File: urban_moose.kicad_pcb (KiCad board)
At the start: 2 copper layers, 27.4 x 49.5 mm, 52 parts, among them P1 SWD, P2 EXT, P3 ANT, Q1 MOSFET_N, Q2 MOSFET_N, SW1 SW_PUSH, U1 nRF51822-QFAA, U2 DS18B20, U3 BMP180, U4 Si1145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

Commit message: Update URL text to um2
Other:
- board text added: "timhawes.com/um2"
- board text removed: "timhawes.com/um1"
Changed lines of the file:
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@@
     )
   )
-  (gr_text timhawes.com/um1 (at 134.62 95.25 90) (layer B.SilkS)
+  (gr_text timhawes.com/um2 (at 134.62 95.25 90) (layer B.SilkS)
     (effects (font (size 1.5 1.5) (thickness 0.3)) (justify mirror))
   )

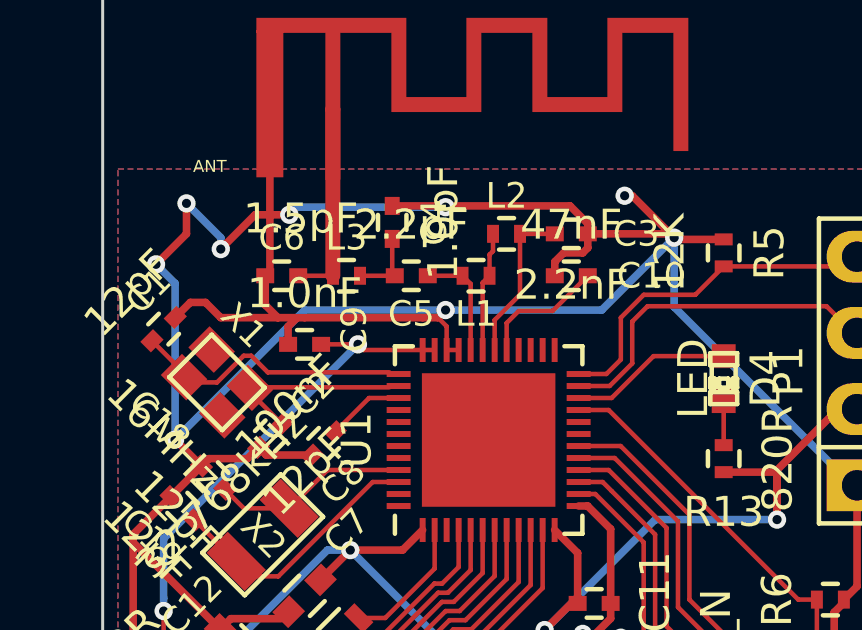
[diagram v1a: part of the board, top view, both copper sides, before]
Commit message: Additional via stitching, track tidy-ups
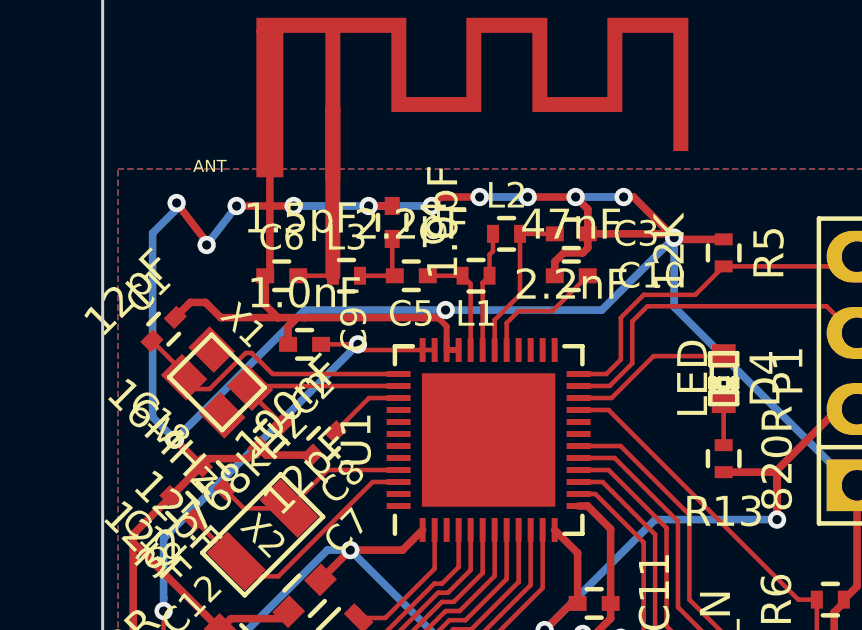
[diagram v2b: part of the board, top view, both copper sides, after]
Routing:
- net GND: track 258.3 -> 259.5 mm, vias 16 -> 20
- net Net-(C1-Pad2): track 9.42 -> 10.3 mm

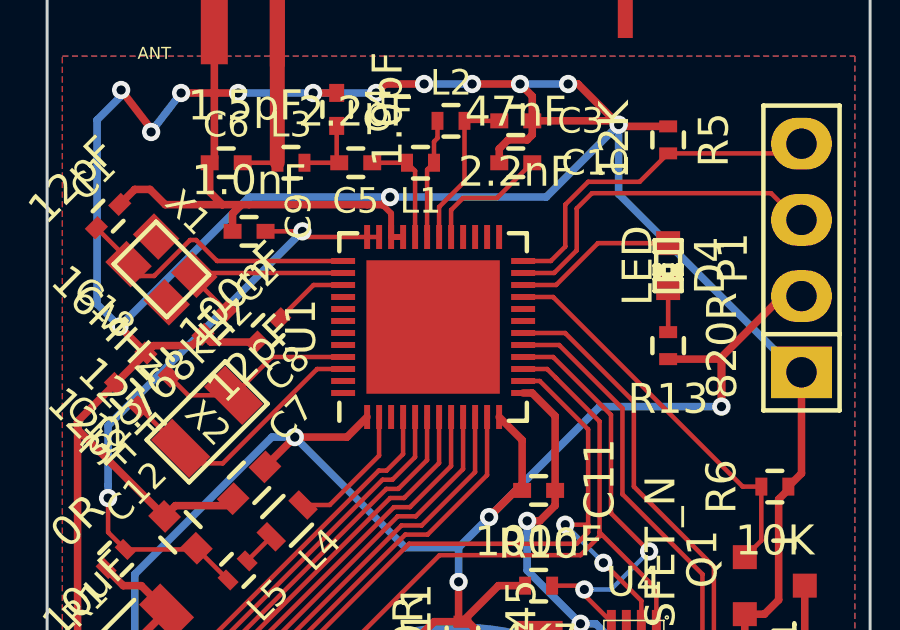
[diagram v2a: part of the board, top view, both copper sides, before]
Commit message: Connect nRF51 centre pad and add vias
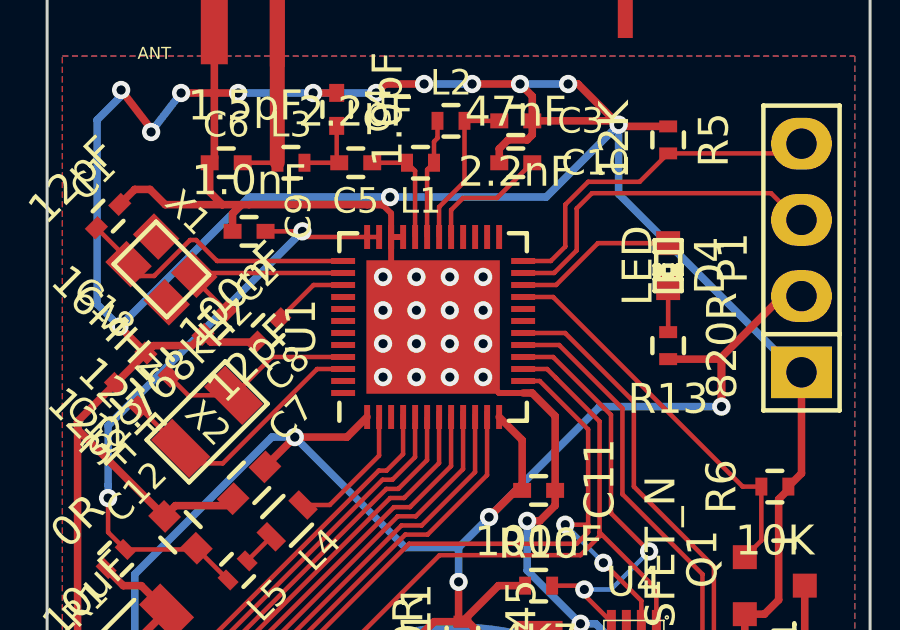
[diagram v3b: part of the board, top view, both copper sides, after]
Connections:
- U1 pad 49: (no net) -> GND
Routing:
- net GND: track 259.5 -> 279.6 mm, vias 20 -> 36
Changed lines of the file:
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@@
 (kicad_pcb (version 4) (host pcbnew 0.201506192325+5795~23~ubuntu14.04.1-product)
   (general
-    (links 124)
+    (links 140)
     (no_connects 1)
     (area 129.983076 75.895999 161.088353 125.526001)
     (thickness 1.6)
     (drawings 5)
-    (tracks 520)
+    (tracks 556)
     (zones 0)
     (modules 52)
@@
     (pad 48 smd rect (at -2.2 -3 180) (size 0.8 0.2) (layers F.Cu F.Paste F.Mask))
     (pad 49 smd rect (at 1.66875 1.66875 90) (size 1.1125 1.1125) (layers F.Cu F.Paste F.Mask)
-      (solder_paste_margin_ratio -0.2))
+      (net 1 GND) (solder_paste_margin_ratio -0.2))
     (pad 49 smd rect (at 1.66875 0.55625 90) (size 1.1125 1.1125) (layers F.Cu F.Paste F.Mask)
-      (solder_paste_margin_ratio -0.2))
+      (net 1 GND) (solder_paste_margin_ratio -0.2))
     (pad 49 smd rect (at 1.66875 -0.55625 90) (size 1.1125 1.1125) (layers F.Cu F.Paste F.Mask)
-      (solder_paste_margin_ratio -0.2))
+      (net 1 GND) (solder_paste_margin_ratio -0.2))
     (pad 49 smd rect (at 1.66875 -1.66875 90) (size 1.1125 1.1125) (layers F.Cu F.Paste F.Mask)
-      (solder_paste_margin_ratio -0.2))
+      (net 1 GND) (solder_paste_margin_ratio -0.2))
     (pad 49 smd rect (at 0.55625 1.66875 90) (size 1.1125 1.1125) (layers F.Cu F.Paste F.Mask)
-      (solder_paste_margin_ratio -0.2))
+      (net 1 GND) (solder_paste_margin_ratio -0.2))
     (pad 49 smd rect (at 0.55625 0.55625 90) (size 1.1125 1.1125) (layers F.Cu F.Paste F.Mask)
-      (solder_paste_margin_ratio -0.2))
+      (net 1 GND) (solder_paste_margin_ratio -0.2))
     (pad 49 smd rect (at 0.55625 -0.55625 90) (size 1.1125 1.1125) (layers F.Cu F.Paste F.Mask)
-      (solder_paste_margin_ratio -0.2))
+      (net 1 GND) (solder_paste_margin_ratio -0.2))
     (pad 49 smd rect (at 0.55625 -1.66875 90) (size 1.1125 1.1125) (layers F.Cu F.Paste F.Mask)
-      (solder_paste_margin_ratio -0.2))
+      (net 1 GND) (solder_paste_margin_ratio -0.2))
     (pad 49 smd rect (at -0.55625 1.66875 90) (size 1.1125 1.1125) (layers F.Cu F.Paste F.Mask)
-      (solder_paste_margin_ratio -0.2))
+      (net 1 GND) (solder_paste_margin_ratio -0.2))
     (pad 49 smd rect (at -0.55625 0.55625 90) (size 1.1125 1.1125) (layers F.Cu F.Paste F.Mask)
-      (solder_paste_margin_ratio -0.2))
+      (net 1 GND) (solder_paste_margin_ratio -0.2))
     (pad 49 smd rect (at -0.55625 -0.55625 90) (size 1.1125 1.1125) (layers F.Cu F.Paste F.Mask)
-      (solder_paste_margin_ratio -0.2))
+      (net 1 GND) (solder_paste_margin_ratio -0.2))
     (pad 49 smd rect (at -0.55625 -1.66875 90) (size 1.1125 1.1125) (layers F.Cu F.Paste F.Mask)
-      (solder_paste_margin_ratio -0.2))
+      (net 1 GND) (solder_paste_margin_ratio -0.2))
     (pad 49 smd rect (at -1.66875 1.66875 90) (size 1.1125 1.1125) (layers F.Cu F.Paste F.Mask)
-      (solder_paste_margin_ratio -0.2))
+      (net 1 GND) (solder_paste_margin_ratio -0.2))
     (pad 49 smd rect (at -1.66875 0.55625 90) (size 1.1125 1.1125) (layers F.Cu F.Paste F.Mask)
-      (solder_paste_margin_ratio -0.2))
+      (net 1 GND) (solder_paste_margin_ratio -0.2))
     (pad 49 smd rect (at -1.66875 -0.55625 90) (size 1.1125 1.1125) (layers F.Cu F.Paste F.Mask)
-      (solder_paste_margin_ratio -0.2))
+      (net 1 GND) (solder_paste_margin_ratio -0.2))
     (pad 49 smd rect (at -1.66875 -1.66875 90) (size 1.1125 1.1125) (layers F.Cu F.Paste F.Mask)
-      (solder_paste_margin_ratio -0.2))
+      (net 1 GND) (solder_paste_margin_ratio -0.2))
     (model Housings_DFN_QFN.3dshapes/UQFN-48-1EP_6x6mm_Pitch0.4mm.wrl
       (at (xyz 0 0 0))
@@
   (gr_line (start 159.766 75.946) (end 159.766 125.476) (layer Edge.Cuts) (width 0.1))
   (gr_line (start 132.334 125.476) (end 132.334 75.946) (layer Edge.Cuts) (width 0.1))
-  (segment (start 144.2 88.2) (end 143.8 88.2) (width 0.2) (layer F.Cu) (net 1) (status C00000))
-  (segment (start 143.8 88.2) (end 143.8 87.412) (width 0.2) (layer F.Cu) (net 1) (status 400000))
+  (segment (start 148.2 93.4) (end 147.4 93.4) (width 0.2) (layer F.Cu) (net 1))
+  (segment (start 147.4 93.4) (end 146.86875 92.86875) (width 0.2) (layer F.Cu) (net 1))
+  (via (at 146.86875 92.86875) (size 0.6096) (drill 0.3048) (layers F.Cu B.Cu) (net 1))
+  (segment (start 146.86875 90.64375) (end 146.86875 91.75625) (width 0.2) (layer B.Cu) (net 1))
+  (via (at 146.86875 90.64375) (size 0.6096) (drill 0.3048) (layers F.Cu B.Cu) (net 1))
+  (via (at 146.86875 89.53125) (size 0.6096) (drill 0.3048) (layers F.Cu B.Cu) (net 1))
+  (segment (start 145.75625 89.53125) (end 146.86875 89.53125) (width 0.2) (layer B.Cu) (net 1))
+  (segment (start 146.86875 89.53125) (end 146.86875 90.64375) (width 0.2) (layer B.Cu) (net 1))
+  (via (at 146.86875 91.75625) (size 0.6096) (drill 0.3048) (layers F.Cu B.Cu) (net 1))
+  (via (at 145.75625 89.53125) (size 0.6096) (drill 0.3048) (layers F.Cu B.Cu) (net 1))
+  (segment (start 146.86875 91.75625) (end 146.86875 92.86875) (width 0.2) (layer B.Cu) (net 1))
+  (via (at 145.75625 92.86875) (size 0.6096) (drill 0.3048) (layers F.Cu B.Cu) (net 1))
+  (segment (start 145.75625 90.64375) (end 145.75625 91.75625) (width 0.2) (layer B.Cu) (net 1))
+  (via (at 145.75625 90.64375) (size 0.6096) (drill 0.3048) (layers F.Cu B.Cu) (net 1))
+  (segment (start 145.75625 89.53125) (end 145.75625 90.64375) (width 0.2) (layer B.Cu) (net 1))
+  (via (at 145.75625 91.75625) (size 0.6096) (drill 0.3048) (layers F.Cu B.Cu) (net 1))
+  (segment (start 145.75625 91.75625) (end 145.75625 92.86875) (width 0.2) (layer B.Cu) (net 1))
+  (via (at 144.64375 92.86875) (size 0.6096) (drill 0.3048) (layers F.Cu B.Cu) (net 1))
+  (segment (start 144.64375 90.64375) (end 144.64375 91.75625) (width 0.2) (layer B.Cu) (net 1))
+  (via (at 144.64375 90.64375) (size 0.6096) (drill 0.3048) (layers F.Cu B.Cu) (net 1))
+  (via (at 144.64375 89.53125) (size 0.6096) (drill 0.3048) (layers F.Cu B.Cu) (net 1))
+  (segment (start 144.64375 89.53125) (end 144.64375 90.64375) (width 0.2) (layer B.Cu) (net 1))
+  (via (at 144.64375 91.75625) (size 0.6096) (drill 0.3048) (layers F.Cu B.Cu) (net 1))
+  (segment (start 144.64375 91.75625) (end 144.64375 92.86875) (width 0.2) (layer B.Cu) (net 1))
+  (via (at 143.53125 92.86875) (size 0.6096) (drill 0.3048) (layers F.Cu B.Cu) (net 1))
+  (segment (start 143.53125 90.64375) (end 143.53125 91.75625) (width 0.2) (layer B.Cu) (net 1))
+  (via (at 143.53125 90.64375) (size 0.6096) (drill 0.3048) (layers F.Cu B.Cu) (net 1))
+  (segment (start 143.53125 89.53125) (end 143.53125 90.64375) (width 0.2) (layer B.Cu) (net 1))
+  (via (at 143.53125 91.75625) (size 0.6096) (drill 0.3048) (layers F.Cu B.Cu) (net 1))
+  (segment (start 143.53125 91.75625) (end 143.53125 92.86875) (width 0.2) (layer B.Cu) (net 1))
+  (via (at 143.53125 89.53125) (size 0.6096) (drill 0.3048) (layers F.Cu B.Cu) (net 1))
+  (segment (start 143.53125 89.53125) (end 144.64375 89.53125) (width 0.2) (layer B.Cu) (net 1))
+  (segment (start 144.64375 89.53125) (end 145.75625 89.53125) (width 0.2) (layer B.Cu) (net 1))
+  (segment (start 143.8 88.2) (end 143.8 89.2625) (width 0.2) (layer F.Cu) (net 1))
+  (segment (start 143.8 89.2625) (end 143.53125 89.53125) (width 0.2) (layer F.Cu) (net 1))
+  (segment (start 143.8 89.2625) (end 143.53125 89.53125) (width 0.2) (layer F.Cu) (net 1))
+  (segment (start 144.2 88.2) (end 143.8 88.2) (width 0.2) (layer F.Cu) (net 1))
+  (segment (start 143.8 88.2) (end 143.8 87.412) (width 0.2) (layer F.Cu) (net 1))
   (segment (start 143.8 87.412) (end 143.51 87.122) (width 0.2) (layer F.Cu) (net 1))
   (segment (start 149.7 83.1) (end 150.029 83.1) (width 0.254) (layer F.Cu) (net 1))

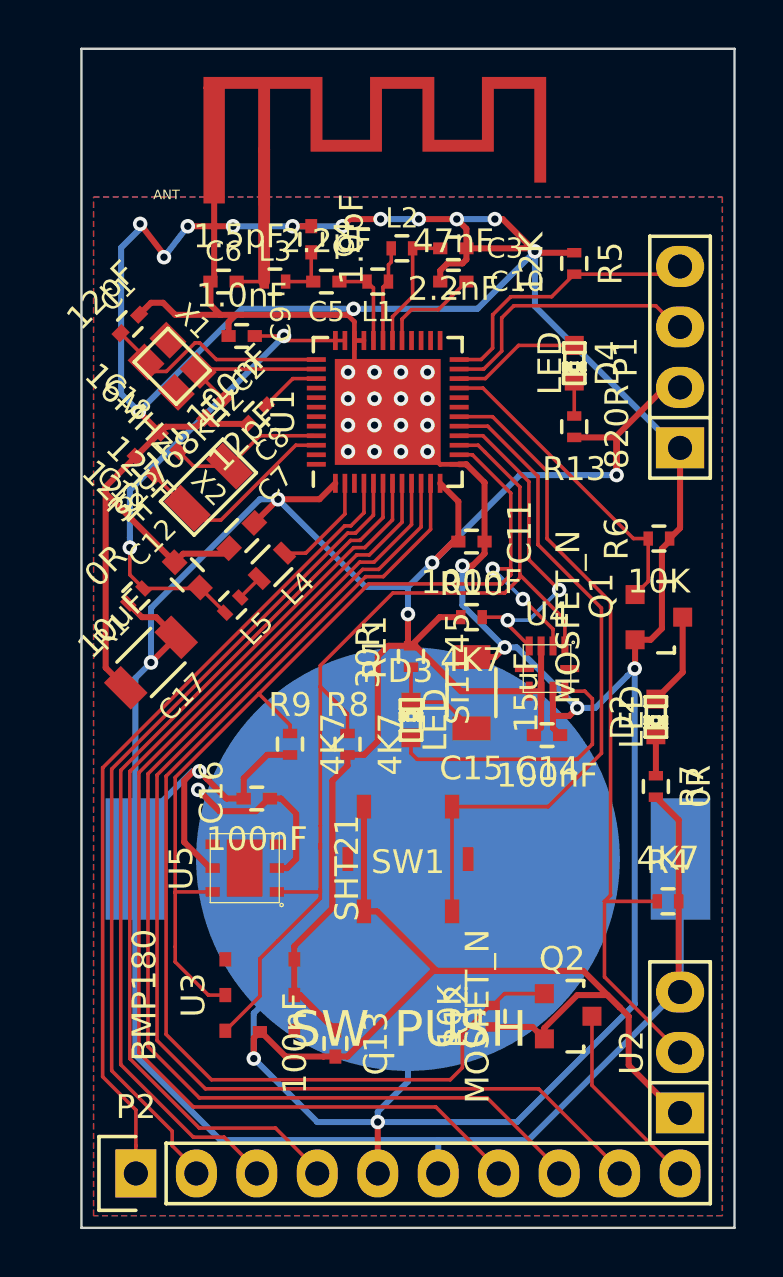
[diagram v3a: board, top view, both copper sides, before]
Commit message: Routing tidy-up
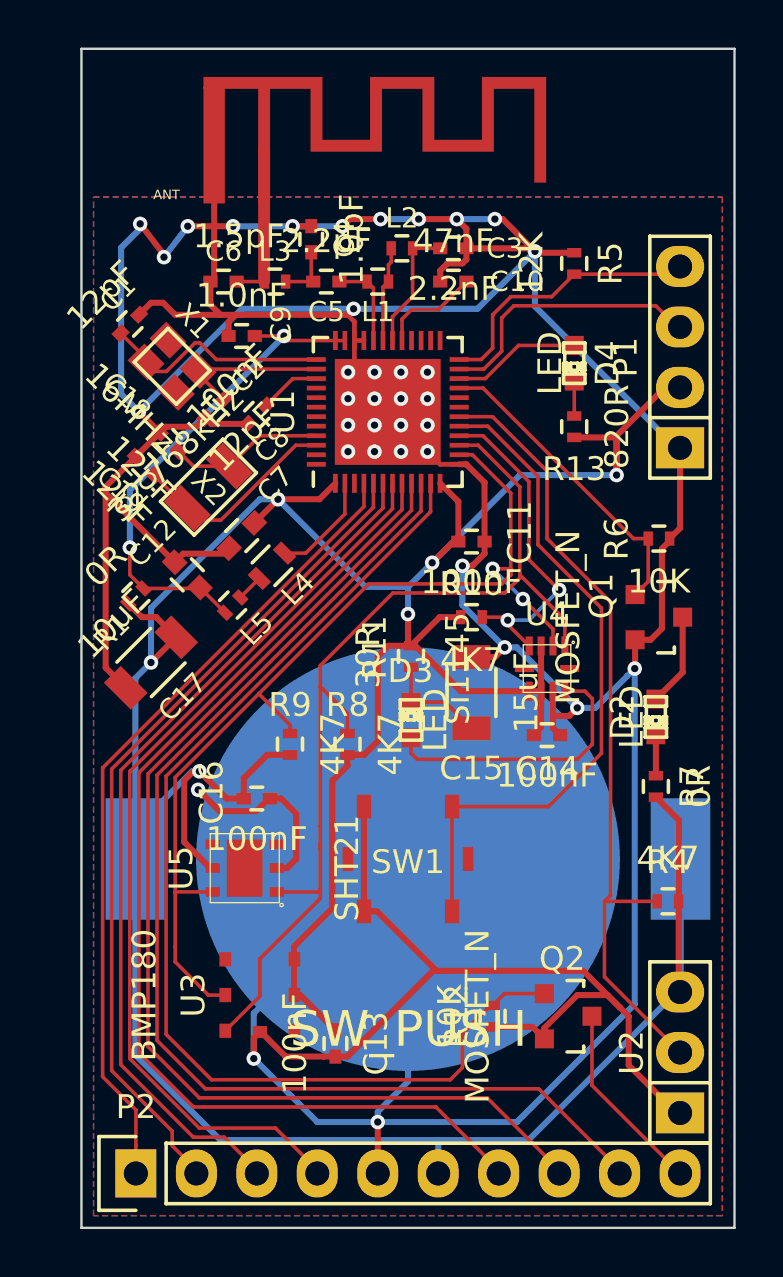
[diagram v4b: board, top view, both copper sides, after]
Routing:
- net FET1: track 47.4 -> 46.8 mm
- net AIN6: track 48.4 -> 47.8 mm

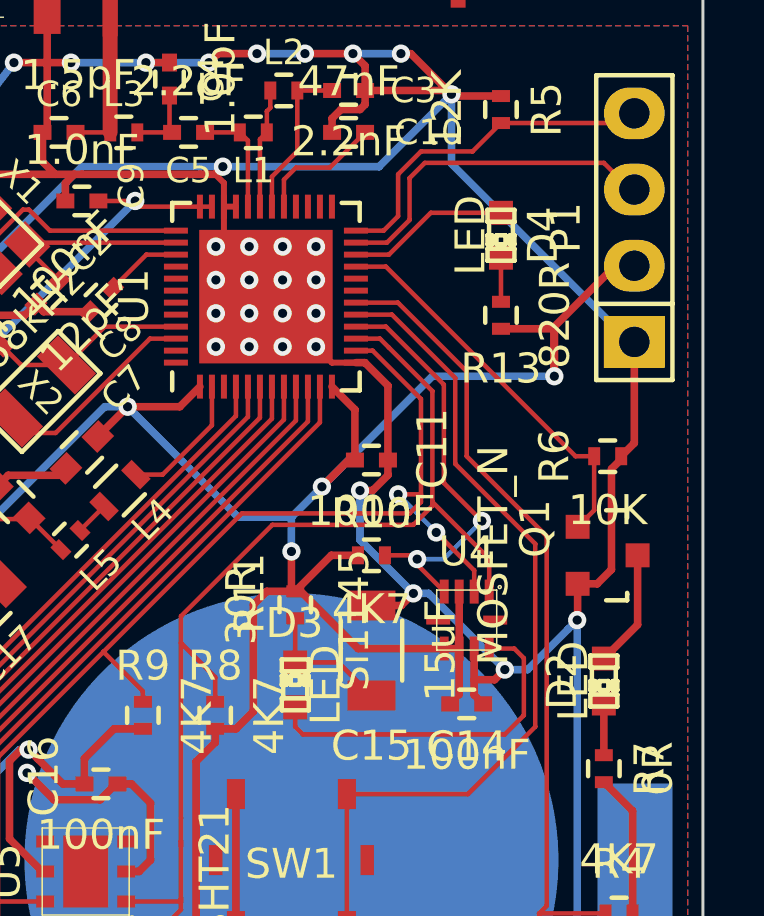
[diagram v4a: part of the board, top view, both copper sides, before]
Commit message: Tidy-up ground pins on nRF51 and replace LED silkscreens
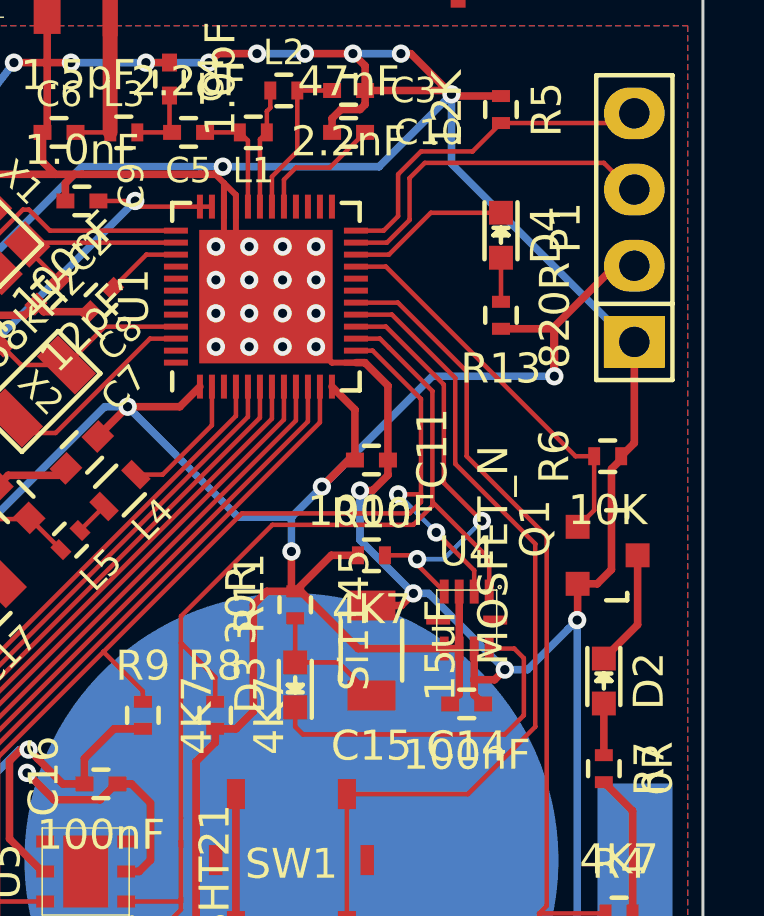
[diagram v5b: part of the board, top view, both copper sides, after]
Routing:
- net GND: track 279.6 -> 281.7 mm
